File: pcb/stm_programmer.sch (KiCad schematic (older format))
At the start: 37 parts

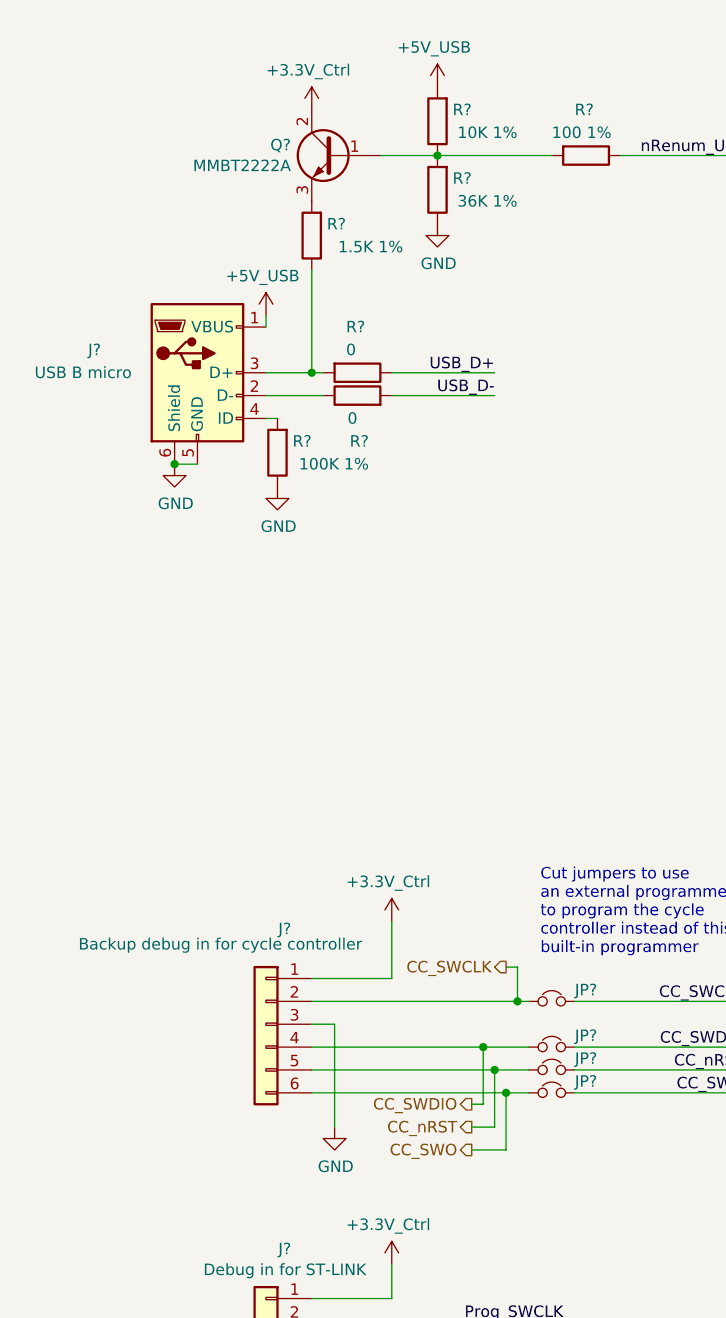
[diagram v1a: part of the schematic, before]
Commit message: Stepper drivers, alarms, power
Broke out SPI pins from cycle controller, routed to stepper drivers
Alarm/alarm battery changes:
(Fixed incorrect use of +BATT instead of +5V_Batt)
(Removed "run FPGA from alarm battery" circuitry and moved alarm battery circuitry to alarms sheet)
Converted fixed power symbols on logic/control power sheet, solenoid driver sheet to hierarchical labels to make power flow more clear from top level
Minor parts consolidation
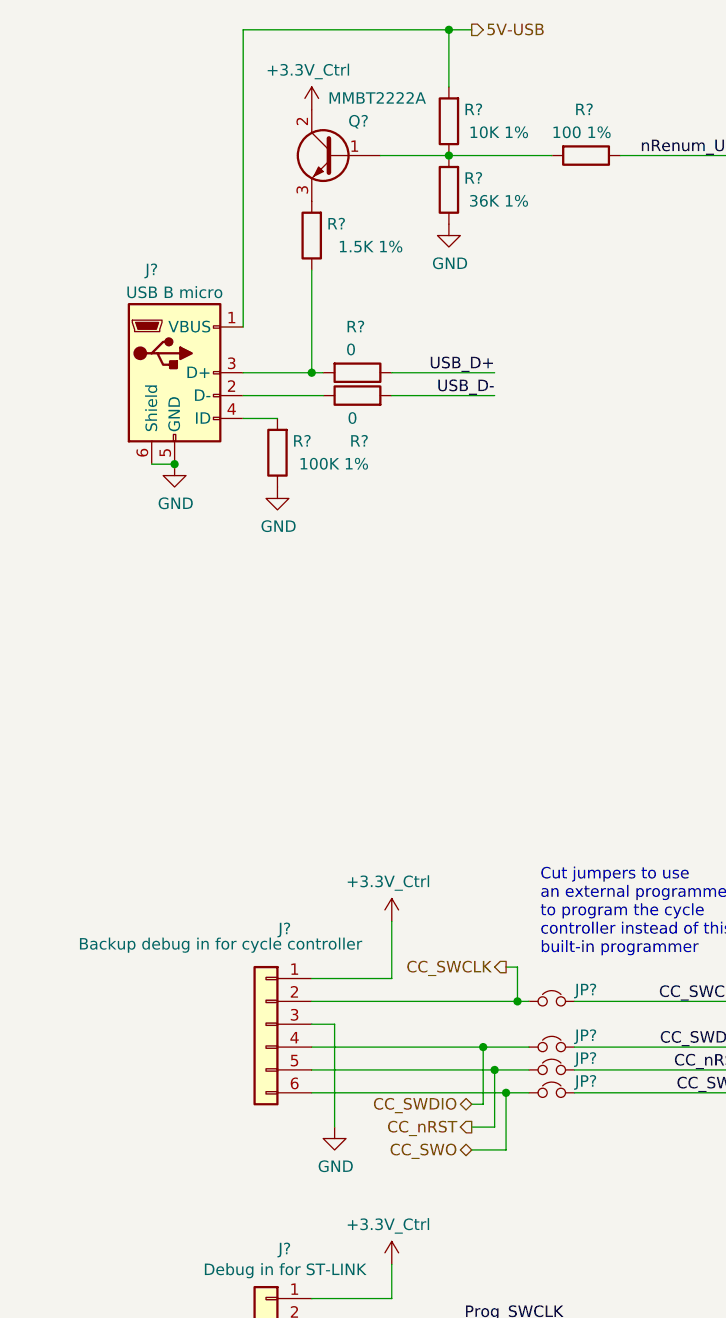
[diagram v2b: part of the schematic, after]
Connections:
- net +5V_USB renamed 5V-USB
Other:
- moved on the sheet: J?, R?
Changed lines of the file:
@@
 $Descr A4 11693 8268
 encoding utf-8
-Sheet 9 37
+Sheet 37 37
 Title "STM Programmer for Cycle Controller"
 Date ""
@@
 L Connector:USB_B_Micro J?
 U 1 1 5FF1A7AE
-P 1250 2500
+P 1150 2500
 AR Path="/5FF1A7AE" Ref="J?"  Part="1"
 AR Path="/5FCD4D85/5FF1A7AE" Ref="J?"  Part="1"
-F 0 "J?" H 800 2600 50  0000 C CNN
-F 1 "USB B micro" H 750 2500 50  0000 C CNN
-F 2 "" H 1400 2450 50  0001 C CNN
-F 3 "~" H 1400 2450 50  0001 C CNN
-	1    1250 2500
+F 0 "J?" H 1050 2950 50  0000 C CNN
+F 1 "USB B micro" H 1150 2850 50  0000 C CNN
+F 2 "" H 1300 2450 50  0001 C CNN
+F 3 "~" H 1300 2450 50  0001 C CNN
+	1    1150 2500
 	1    0    0    -1
 $EndComp
@@
 	1    0    0    -1
 $EndComp
-Wire Wire Line
-	1150 2900 1250 2900
 Connection ~ 1150 2900
 $Comp
@@
 	-1   0    0    1
 $EndComp
-Wire Wire Line
-	1600 2700 1550 2700
 $Comp
 L power:GND #PWR?
@@
 Wire Wire Line
 	1800 2500 1750 2500
-Wire Wire Line
-	1550 2600 1800 2600
 Text Label 2550 2600 2    50   ~ 0
 USB_D-
@@
 	1750 2050 1750 2500
 Connection ~ 1750 2500
-Wire Wire Line
-	1750 2500 1550 2500
 $Comp
 L Device:Q_NPN_BCE Q?
 U 1 1 5FF31A97
 P 1850 1550
-F 0 "Q?" H 2041 1596 50  0000 L CNN
-F 1 "MMBT2222A" H 2041 1505 50  0000 L CNN
+F 0 "Q?" H 1700 1700 50  0000 L CNN
+F 1 "MMBT2222A" H 1450 1800 50  0000 L CNN
 F 2 "RespiraWorks_Std:SOT-23" H 2050 1650 50  0001 C CNN
 F 3 "~" H 1850 1550 50  0001 C CNN
@@
 L Device:R R?
 U 1 1 5FF3BDCF
-P 2300 1400
+P 2350 1400
 AR Path="/5FCD4B8E/5FCD4BC5/5FF3BDCF" Ref="R?"  Part="1"
 AR Path="/5FCD4B8E/5FE27F70/5FF3BDCF" Ref="R?"  Part="1"
 AR Path="/5FCD4D85/5FF3BDCF" Ref="R?"  Part="1"
-F 0 "R?" H 2150 1350 50  0000 L CNN
-F 1 "10K 1%" H 1950 1450 50  0000 L CNN
-F 2 "RespiraWorks_Std:R_0603_1608Metric" V 2230 1400 50  0001 C CNN
-F 3 "~" H 2300 1400 50  0001 C CNN
-	1    2300 1400
+F 0 "R?" H 2200 1350 50  0000 L CNN
+F 1 "10K 1%" H 2000 1450 50  0000 L CNN
+F 2 "RespiraWorks_Std:R_0603_1608Metric" V 2280 1400 50  0001 C CNN
+F 3 "~" H 2350 1400 50  0001 C CNN
+	1    2350 1400
 	-1   0    0    1
 $EndComp
@@
 L Device:R R?
 U 1 1 5FF3C26A
-P 2300 1700
+P 2350 1700
 AR Path="/5FCD4B8E/5FCD4BC5/5FF3C26A" Ref="R?"  Part="1"
 AR Path="/5FCD4B8E/5FE27F70/5FF3C26A" Ref="R?"  Part="1"
 AR Path="/5FCD4D85/5FF3C26A" Ref="R?"  Part="1"
-F 0 "R?" H 2150 1650 50  0000 L CNN
-F 1 "36K 1%" H 1950 1750 50  0000 L CNN
-F 2 "RespiraWorks_Std:R_0603_1608Metric" V 2230 1700 50  0001 C CNN
-F 3 "~" H 2300 1700 50  0001 C CNN
-	1    2300 1700
-	-1   0    0    1
-$EndComp
-Wire Wire Line
-	2050 1550 2300 1550
-Connection ~ 2300 1550
+F 0 "R?" H 2200 1650 50  0000 L CNN
+F 1 "36K 1%" H 2000 1750 50  0000 L CNN
+F 2 "RespiraWorks_Std:R_0603_1608Metric" V 2280 1700 50  0001 C CNN
+F 3 "~" H 2350 1700 50  0001 C CNN
+	1    2350 1700
+	-1   0    0    1
+$EndComp
+Wire Wire Line
+	2050 1550 2350 1550
+Connection ~ 2350 1550
 $Comp
 L power:GND #PWR?
 U 1 1 5FF3DB70
-P 2300 1850
+P 2350 1850
 AR Path="/5FCD4B8E/5FCD4BC5/5FF3DB70" Ref="#PWR?"  Part="1"
 AR Path="/5FCD4B8E/5FE27F70/5FF3DB70" Ref="#PWR?"  Part="1"
 AR Path="/5FCD4D85/5FF3DB70" Ref="#PWR?"  Part="1"
-F 0 "#PWR?" H 2300 1600 50  0001 C CNN
-F 1 "GND" H 2305 1677 50  0000 C CNN
-F 2 "" H 2300 1850 50  0001 C CNN
-F 3 "" H 2300 1850 50  0001 C CNN
-	1    2300 1850
+F 0 "#PWR?" H 2350 1600 50  0001 C CNN
+F 1 "GND" H 2355 1677 50  0000 C CNN
+F 2 "" H 2350 1850 50  0001 C CNN
+F 3 "" H 2350 1850 50  0001 C CNN
+	1    2350 1850
 	1    0    0    -1
 $EndComp
@@
 $EndComp
 Wire Wire Line
-	2800 1550 2300 1550
+	2800 1550 2350 1550
 Text Label 3650 1550 2    50   ~ 0
 nRenum_USB
@@
 $EndComp
 $Comp
-L RespiraWorks:+5V_USB #PWR?
-U 1 1 5FFFC08C
-P 1550 2250
-F 0 "#PWR?" H 1550 2250 50  0001 C CNN
-F 1 "+5V_USB" H 1535 2423 50  0000 C CNN
-F 2 "" H 1550 2250 50  0001 C CNN
-F 3 "" H 1550 2250 50  0001 C CNN
-	1    1550 2250
-	1    0    0    -1
-$EndComp
-Wire Wire Line
-	1550 2250 1550 2300
-$Comp
-L RespiraWorks:+5V_USB #PWR?
-U 1 1 5FFFF9F0
-P 2300 1250
-F 0 "#PWR?" H 2300 1250 50  0001 C CNN
-F 1 "+5V_USB" H 2285 1423 50  0000 C CNN
-F 2 "" H 2300 1250 50  0001 C CNN
-F 3 "" H 2300 1250 50  0001 C CNN
-	1    2300 1250
-	1    0    0    -1
-$EndComp
-$Comp
 L RespiraWorks:+3.3V_Ctrl #PWR?
 U 1 1 6000178D
@@
 Text HLabel 2600 5100 0    50   Output ~ 0
 CC_SWCLK
-Text HLabel 2450 5700 0    50   Output ~ 0
+Text HLabel 2450 5700 0    50   BiDi ~ 0
 CC_SWDIO
 Text HLabel 2450 5800 0    50   Output ~ 0
 CC_nRST
-Text HLabel 2450 5900 0    50   Output ~ 0
+Text HLabel 2450 5900 0    50   BiDi ~ 0
 CC_SWO
 Wire Wire Line
@@
 Wire Wire Line
 	8450 2550 9000 2550
+Text HLabel 2450 1000 2    50   Output ~ 0
+5V-USB
+Wire Wire Line
+	1450 1000 2350 1000
+Wire Wire Line
+	1450 1000 1450 2300
+Wire Wire Line
+	2350 1250 2350 1000
+Connection ~ 2350 1000
+Wire Wire Line
+	2350 1000 2450 1000
+Wire Wire Line
+	1450 2500 1750 2500
+Wire Wire Line
+	1450 2600 1800 2600
+Wire Wire Line
+	1450 2700 1600 2700
+Wire Wire Line
+	1150 2900 1050 2900
 $EndSCHEMATC

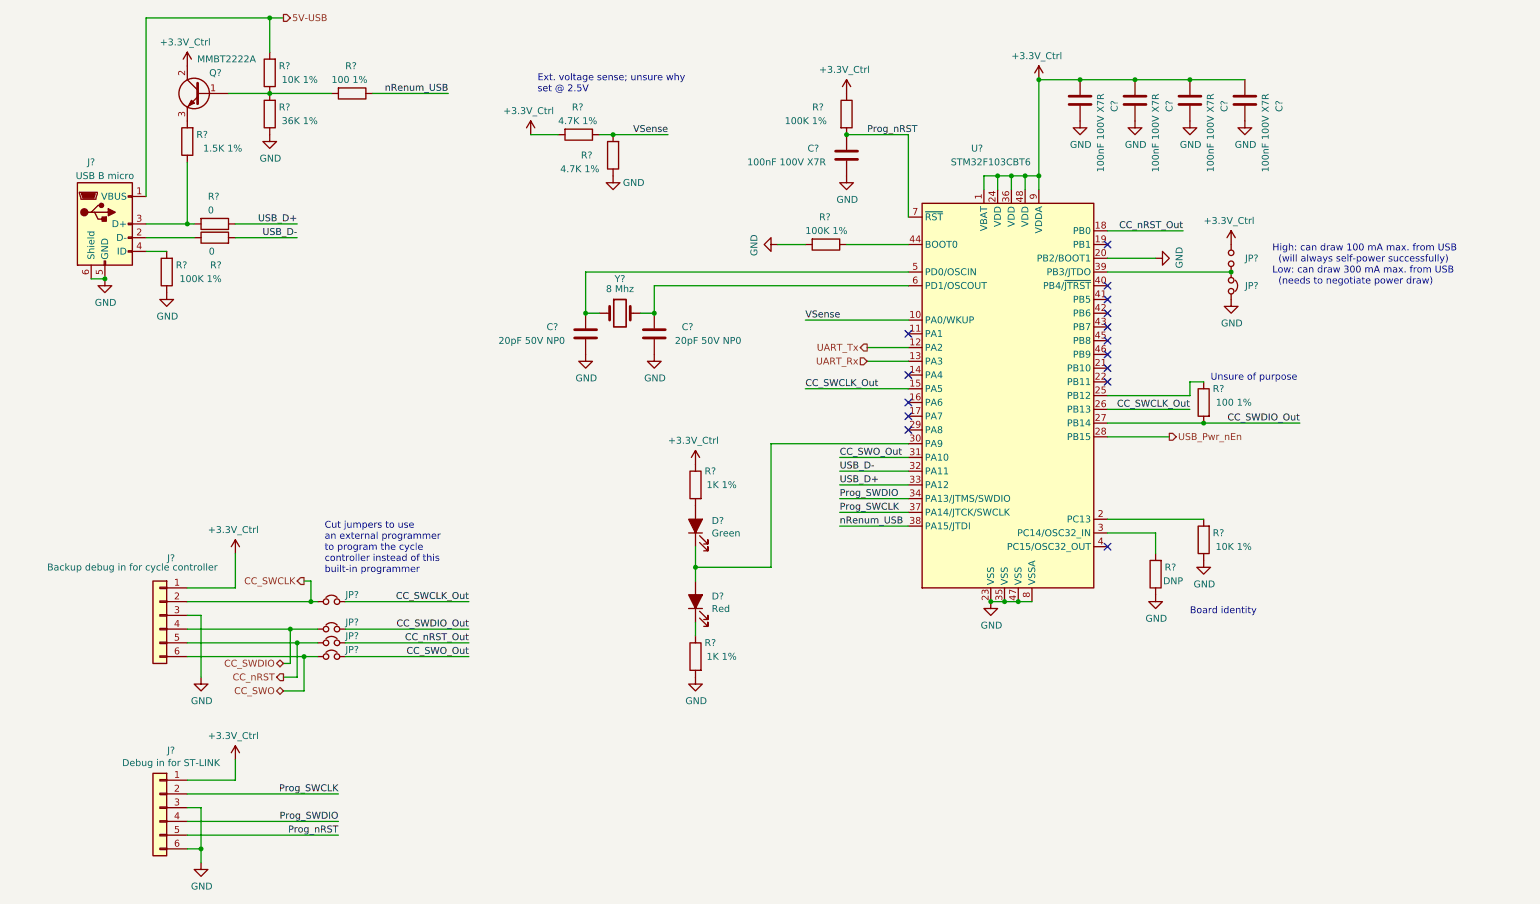
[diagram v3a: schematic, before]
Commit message: CC-I2C, BOM
Added missing pull-ups on CC-SDA, CC-SCL
First pass at BOM consolidation
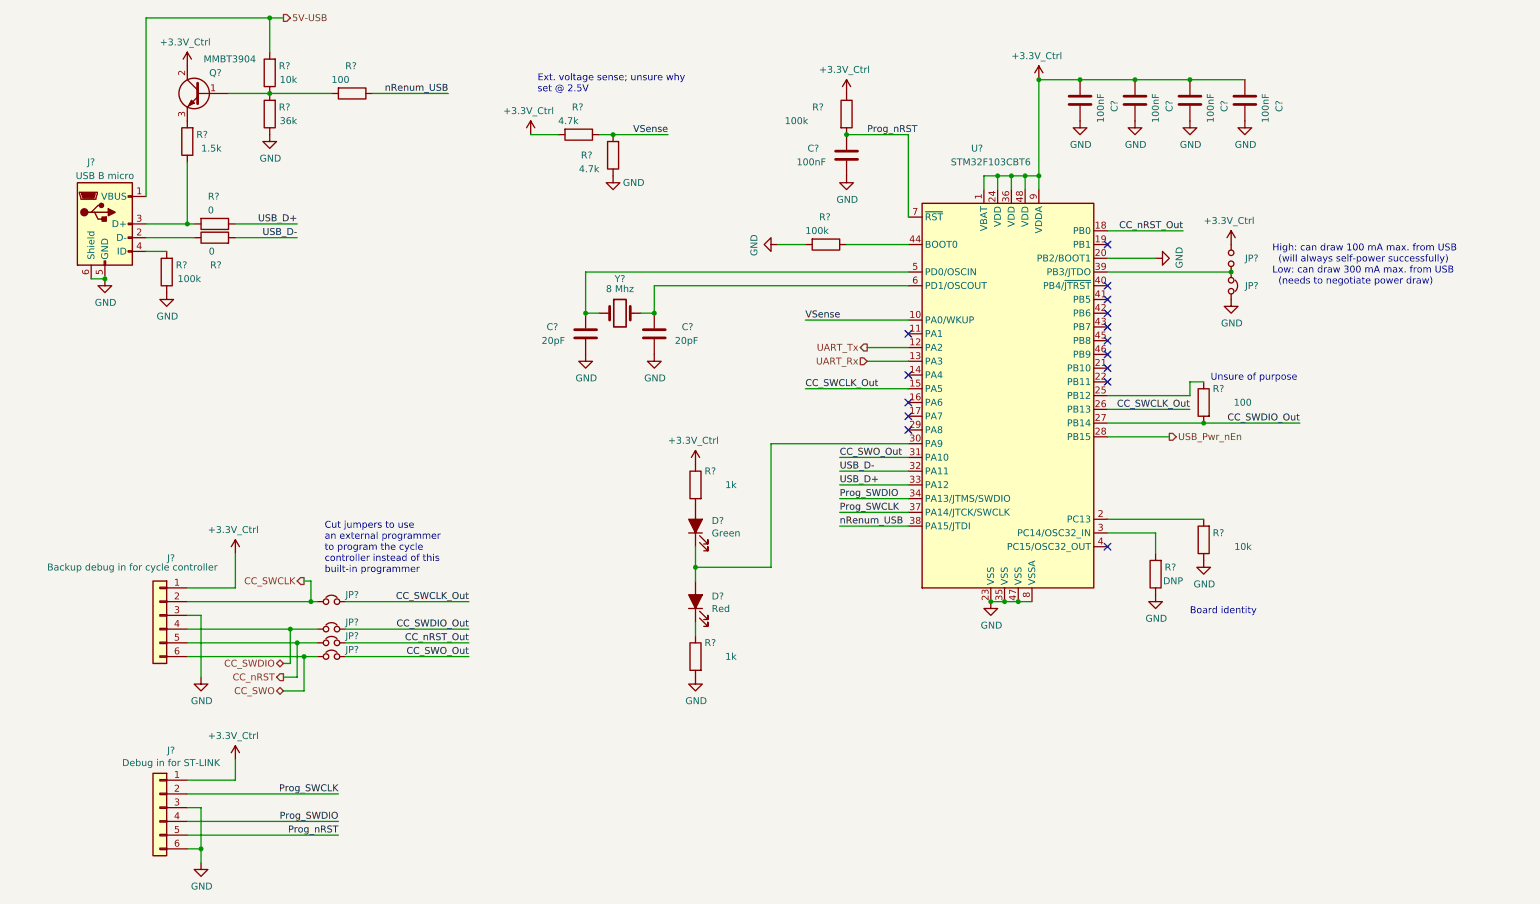
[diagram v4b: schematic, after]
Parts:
- C? (x5): value 100nF 100V X7R -> 100nF
- C? (x2): value 20pF 50V NP0 -> 20pF
- Q?: value MMBT2222A -> MMBT3904
- R? (x3): value 100K 1% -> 100k
- R? (x2): value 100 1% -> 100
- R? (x2): footprint RespiraWorks_Std:R_0603_1608Metric -> RespiraWorks_std:R_0603_1608Metric
- R?: value 1.5K 1% -> 1.5k
- R? (x2): value 10K 1% -> 10k
- R?: value 36K 1% -> 36k
- R? (x2): value 1K 1% -> 1k
- R? (x2): value 4.7K 1% -> 4.7k
- R?: DNP (none) -> DNP
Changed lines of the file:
@@
 AR Path="/5FCD4D85/5FEF0F3B" Ref="C?"  Part="1"
 F 0 "C?" V 8000 1600 50  0000 L CNN
-F 1 "100nF 100V X7R" V 8100 1550 50  0000 L CNN
+F 1 "100nF" V 8100 1550 50  0000 L CNN
 F 2 "RespiraWorks_Std:C_0603_1608Metric" H 8288 1450 50  0001 C CNN
 F 3 "~" H 8250 1600 50  0001 C CNN
@@
 AR Path="/5FCD4D85/5FEF14C7" Ref="C?"  Part="1"
 F 0 "C?" V 8400 1600 50  0000 L CNN
-F 1 "100nF 100V X7R" V 8500 1550 50  0000 L CNN
+F 1 "100nF" V 8500 1550 50  0000 L CNN
 F 2 "RespiraWorks_Std:C_0603_1608Metric" H 8688 1450 50  0001 C CNN
 F 3 "~" H 8650 1600 50  0001 C CNN
@@
 AR Path="/5FCD4D85/5FEF1925" Ref="C?"  Part="1"
 F 0 "C?" V 8800 1600 50  0000 L CNN
-F 1 "100nF 100V X7R" V 8900 1550 50  0000 L CNN
+F 1 "100nF" V 8900 1550 50  0000 L CNN
 F 2 "RespiraWorks_Std:C_0603_1608Metric" H 9088 1450 50  0001 C CNN
 F 3 "~" H 9050 1600 50  0001 C CNN
@@
 AR Path="/5FCD4D85/5FEF1DD5" Ref="C?"  Part="1"
 F 0 "C?" V 9200 1600 50  0000 L CNN
-F 1 "100nF 100V X7R" V 9300 1550 50  0000 L CNN
+F 1 "100nF" V 9300 1550 50  0000 L CNN
 F 2 "RespiraWorks_Std:C_0603_1608Metric" H 9488 1450 50  0001 C CNN
 F 3 "~" H 9450 1600 50  0001 C CNN
@@
 AR Path="/5FCD4D85/5FEF4F07" Ref="C?"  Part="1"
 F 0 "C?" H 6750 1950 50  0000 L CNN
-F 1 "100nF 100V X7R" H 6700 2050 50  0000 L CNN
+F 1 "100nF" H 6700 2050 50  0000 L CNN
 F 2 "RespiraWorks_Std:C_0603_1608Metric" H 6588 1850 50  0001 C CNN
 F 3 "~" H 6550 2000 50  0001 C CNN
@@
 AR Path="/5FCD4D85/5FEFCD09" Ref="R?"  Part="1"
 F 0 "R?" H 6300 1750 50  0000 L CNN
-F 1 "100K 1%" H 6100 1650 50  0000 L CNN
+F 1 "100k" H 6100 1650 50  0000 L CNN
 F 2 "RespiraWorks_Std:R_0603_1608Metric" V 6480 1700 50  0001 C CNN
 F 3 "~" H 6550 1700 50  0001 C CNN
@@
 AR Path="/5FCD4D85/5FF0A33E" Ref="R?"  Part="1"
 F 0 "R?" H 9000 3900 50  0000 L CNN
-F 1 "100 1%" H 8800 3800 50  0000 L CNN
+F 1 "100" H 8800 3800 50  0000 L CNN
 F 2 "RespiraWorks_Std:R_0603_1608Metric" V 9080 3800 50  0001 C CNN
 F 3 "~" H 9150 3800 50  0001 C CNN
@@
 AR Path="/5FCD4D85/5FF10D79" Ref="R?"  Part="1"
 F 0 "R?" V 6200 2600 50  0000 L CNN
-F 1 "100K 1%" V 6300 2500 50  0000 L CNN
+F 1 "100k" V 6300 2500 50  0000 L CNN
 F 2 "RespiraWorks_Std:R_0603_1608Metric" V 6330 2650 50  0001 C CNN
 F 3 "~" H 6400 2650 50  0001 C CNN
@@
 AR Path="/5FCD4D85/5FF24FD8" Ref="R?"  Part="1"
 F 0 "R?" H 1450 2800 50  0000 L CNN
-F 1 "100K 1%" H 1200 2900 50  0000 L CNN
+F 1 "100k" H 1350 2900 50  0000 L CNN
 F 2 "RespiraWorks_Std:R_0603_1608Metric" V 1530 2850 50  0001 C CNN
 F 3 "~" H 1600 2850 50  0001 C CNN
@@
 F 0 "R?" V 1750 2450 50  0000 L CNN
 F 1 "0" V 1850 2450 50  0000 L CNN
-F 2 "RespiraWorks_Std:R_0603_1608Metric" V 1880 2500 50  0001 C CNN
+F 2 "RespiraWorks_std:R_0603_1608Metric" V 1880 2500 50  0001 C CNN
 F 3 "~" H 1950 2500 50  0001 C CNN
 	1    1950 2500
@@
 F 0 "R?" V 1750 2550 50  0000 L CNN
 F 1 "0" V 1850 2600 50  0000 L CNN
-F 2 "RespiraWorks_Std:R_0603_1608Metric" V 1880 2600 50  0001 C CNN
+F 2 "RespiraWorks_std:R_0603_1608Metric" V 1880 2600 50  0001 C CNN
 F 3 "~" H 1950 2600 50  0001 C CNN
 	1    1950 2600
@@
 AR Path="/5FCD4D85/5FF302E3" Ref="R?"  Part="1"
 F 0 "R?" H 1600 1850 50  0000 L CNN
-F 1 "1.5K 1%" H 1350 1950 50  0000 L CNN
+F 1 "1.5k" H 1500 1950 50  0000 L CNN
 F 2 "RespiraWorks_Std:R_0603_1608Metric" V 1680 1900 50  0001 C CNN
 F 3 "~" H 1750 1900 50  0001 C CNN
@@
 P 1850 1550
 F 0 "Q?" H 1700 1700 50  0000 L CNN
-F 1 "MMBT2222A" H 1450 1800 50  0000 L CNN
+F 1 "MMBT3904" H 1450 1800 50  0000 L CNN
 F 2 "RespiraWorks_Std:SOT-23" H 2050 1650 50  0001 C CNN
 F 3 "~" H 1850 1550 50  0001 C CNN
@@
 AR Path="/5FCD4D85/5FF3BDCF" Ref="R?"  Part="1"
 F 0 "R?" H 2200 1350 50  0000 L CNN
-F 1 "10K 1%" H 2000 1450 50  0000 L CNN
+F 1 "10k" H 2150 1450 50  0000 L CNN
 F 2 "RespiraWorks_Std:R_0603_1608Metric" V 2280 1400 50  0001 C CNN
 F 3 "~" H 2350 1400 50  0001 C CNN
@@
 AR Path="/5FCD4D85/5FF3C26A" Ref="R?"  Part="1"
 F 0 "R?" H 2200 1650 50  0000 L CNN
-F 1 "36K 1%" H 2000 1750 50  0000 L CNN
+F 1 "36k" H 2150 1750 50  0000 L CNN
 F 2 "RespiraWorks_Std:R_0603_1608Metric" V 2280 1700 50  0001 C CNN
 F 3 "~" H 2350 1700 50  0001 C CNN
@@
 AR Path="/5FCD4D85/5FF418B2" Ref="R?"  Part="1"
 F 0 "R?" V 2750 1500 50  0000 L CNN
-F 1 "100 1%" V 2850 1400 50  0000 L CNN
+F 1 "100" V 2850 1400 50  0000 L CNN
 F 2 "RespiraWorks_Std:R_0603_1608Metric" V 2880 1550 50  0001 C CNN
 F 3 "~" H 2950 1550 50  0001 C CNN
@@
 AR Path="/5FCD4D85/5FF56FF1" Ref="C?"  Part="1"
 F 0 "C?" H 4850 3250 50  0000 L CNN
-F 1 "20pF 50V NP0" H 4800 3350 50  0000 L CNN
+F 1 "20pF" H 4800 3350 50  0000 L CNN
 F 2 "RespiraWorks_Std:C_0603_1608Metric" H 4688 3150 50  0001 C CNN
 F 3 "~" H 4650 3300 50  0001 C CNN
@@
 AR Path="/5FCD4D85/5FF5ADBF" Ref="C?"  Part="1"
 F 0 "C?" H 5350 3250 50  0000 L CNN
-F 1 "20pF 50V NP0" H 5300 3350 50  0000 L CNN
+F 1 "20pF" H 5300 3350 50  0000 L CNN
 F 2 "RespiraWorks_Std:C_0603_1608Metric" H 5188 3150 50  0001 C CNN
 F 3 "~" H 5150 3300 50  0001 C CNN
@@
 AR Path="/5FCD4D85/5FFEED71" Ref="R?"  Part="1"
 F 0 "R?" H 5300 4500 50  0000 L CNN
-F 1 "1K 1%" H 5150 4400 50  0000 L CNN
+F 1 "1k" H 5150 4400 50  0000 L CNN
 F 2 "RespiraWorks_Std:R_0603_1608Metric" V 5380 4400 50  0001 C CNN
 F 3 "~" H 5450 4400 50  0001 C CNN
@@
 AR Path="/5FCD4D85/5FFEF31C" Ref="R?"  Part="1"
 F 0 "R?" H 5300 5750 50  0000 L CNN
-F 1 "1K 1%" H 5150 5650 50  0000 L CNN
+F 1 "1k" H 5150 5650 50  0000 L CNN
 F 2 "RespiraWorks_Std:R_0603_1608Metric" V 5380 5650 50  0001 C CNN
 F 3 "~" H 5450 5650 50  0001 C CNN
@@
 AR Path="/5FCD4D85/60068022" Ref="R?"  Part="1"
 F 0 "R?" V 4400 1800 50  0000 L CNN
-F 1 "4.7K 1%" V 4500 1700 50  0000 L CNN
+F 1 "4.7k" V 4500 1700 50  0000 L CNN
 F 2 "RespiraWorks_Std:R_0603_1608Metric" V 4530 1850 50  0001 C CNN
 F 3 "~" H 4600 1850 50  0001 C CNN
@@
 AR Path="/5FCD4D85/600684BF" Ref="R?"  Part="1"
 F 0 "R?" H 5000 2000 50  0000 L CNN
-F 1 "4.7K 1%" H 4950 2100 50  0000 L CNN
+F 1 "4.7k" H 4950 2100 50  0000 L CNN
 F 2 "RespiraWorks_Std:R_0603_1608Metric" V 4780 2000 50  0001 C CNN
 F 3 "~" H 4850 2000 50  0001 C CNN
@@
 AR Path="/5FCD4D85/6007ED35" Ref="R?"  Part="1"
 F 0 "R?" H 9000 4750 50  0000 L CNN
-F 1 "10K 1%" H 8800 4850 50  0000 L CNN
+F 1 "10k" H 8800 4850 50  0000 L CNN
 F 2 "RespiraWorks_Std:R_0603_1608Metric" V 9080 4800 50  0001 C CNN
 F 3 "~" H 9150 4800 50  0001 C CNN
@@
 F 2 "RespiraWorks_Std:R_0603_1608Metric" V 8730 5050 50  0001 C CNN
 F 3 "~" H 8800 5050 50  0001 C CNN
+F 4 "DNP" H 8800 5050 50  0001 C CNN "DNP"
 	1    8800 5050
 	-1   0    0    1
